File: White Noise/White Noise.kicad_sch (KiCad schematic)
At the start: 7 parts, among them J101 Conn_02x05_Odd_Even

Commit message: Finish main set of revisions
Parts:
- removed C101, C102: 1u, Capacitor_THT:C_Disc_D5.0mm_W2.5mm_P5.00mm, symbol Device:C
- removed D101, D102: 1N5819, Diode_THT:D_DO-41_SOD81_P10.16mm_Horizontal, symbol Diode:1N5819
- removed J101: Conn_02x05_Odd_Even, Connector_PinHeader_2.54mm:PinHeader_2x05_P2.54mm_Vertical, symbol Connector_Generic:Conn_02x05_Odd_Even
- removed R101, R102: 10, Resistor_THT:R_Axial_DIN0207_L6.3mm_D2.5mm_P7.62mm_Horizontal, symbol Device:R
- added C1, C2: 10u, 0_Capacitor_THT:C_Disc_D5.5mm_W4.0mm_P2.50mm, symbol Device:C
- added C3, C4: 0.1u, 0_Capacitor_THT:C_Disc_D5.5mm_W2.5mm_P2.50mm, symbol Device:C
- added C5: 100u, Capacitor_THT:CP_Radial_D5.0mm_P2.00mm, symbol Device:C_Polarized
- added C6: 10n, 0_Capacitor_THT:C_Disc_D5.5mm_W2.5mm_P2.50mm, symbol Device:C
- added C7, C8: 220n, 0_Capacitor_THT:C_Disc_D5.5mm_W2.5mm_P2.50mm, symbol Device:C
- added D1, D2: 1N5819, Diode_THT:D_DO-41_SOD81_P10.16mm_Horizontal, symbol Diode:1N5819
- added J1: Conn_02x05_Top_Bottom, Connector_Molex:Molex_Mini-Fit_Jr_5566-10A_2x05_P4.20mm_Vertical, symbol Connector_Generic:Conn_02x05_Top_Bottom
- added J2: AudioJack2_SwitchT, Connector_Audio:Jack_3.5mm_QingPu_WQP-PJ398SM_Vertical_CircularHoles, symbol Connector_Audio:AudioJack2_SwitchT
- added Q1: BC548, Package_TO_SOT_THT:TO-92_HandSolder, symbol Transistor_BJT:BC548
- added R1, R4, R6: 4.7k, Resistor_THT:R_Axial_DIN0207_L6.3mm_D2.5mm_P7.62mm_Horizontal, symbol Device:R
- added R2, R3, R5: 100k, Resistor_THT:R_Axial_DIN0207_L6.3mm_D2.5mm_P7.62mm_Horizontal, symbol Device:R
- added R7: 1k, Resistor_THT:R_Axial_DIN0207_L6.3mm_D2.5mm_P7.62mm_Horizontal, symbol Device:R
- added RV1: 50k, 0_Potentiometer_THT:Potentiometer_Alpha_RD901F-40-00D_Single_Vertical_MP, symbol Device:R_Potentiometer_MountingPin
- added U1: TL072, Package_DIP:DIP-8_W7.62mm_Socket, symbol Amplifier_Operational:TL072
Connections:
- net +12V: now also C1.1, C3.2, D1.1 (K), J1.1 (Pin_1), J1.6 (Pin_6), R1.1, U1.8 (V+)
- net -12V: now also C2.2, C4.1, D2.2 (A), J1.10 (Pin_10), J1.5 (Pin_5), U1.4 (V-)
- net GND: now also C1.2, C2.1, C3.1, C4.2, C5.2, C7.1, C8.1, D1.2 (A), D2.1 (K), J1.2 (Pin_2), J1.4 (Pin_4), J1.7 (Pin_7), J1.9 (Pin_9), Q1.2 (B), R3.2
- new net: C5.1, R1.2, R2.1
- new net: C7.2, R4.2
- new net: R4.1, R5.1, U1.2 (-)
- new net: C6.1, Q1.3 (E), R2.2
- new net: R6.1, RV1.1, U1.6 (-)
- new net: R7.1, RV1.2, RV1.3, U1.7
- new net: C8.2, R6.2
- new net: J2.T, R7.2
- new net: R5.2, U1.1, U1.5 (+)
- new net: C6.2, R3.1, U1.3 (+)
- new net Chassis: J1.3 (Pin_3), J1.8 (Pin_8), J2.S, RV1.MP (MountPin)
- no-connect marks 0 -> 2
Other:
- removed sheet Single Source 1

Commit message: Begin revised delay
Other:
- moved on the sheet: C1, C2, C3, C4, C5, C6, C7, C8, D1, D2, J1, J2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

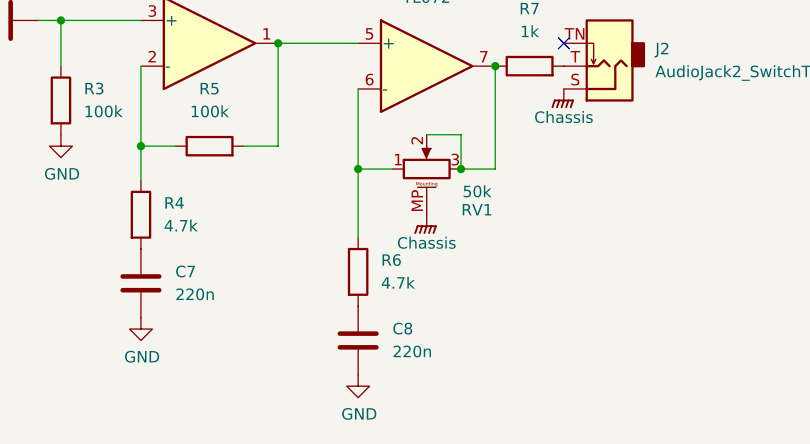
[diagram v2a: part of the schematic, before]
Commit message: Finish diode ladder filter
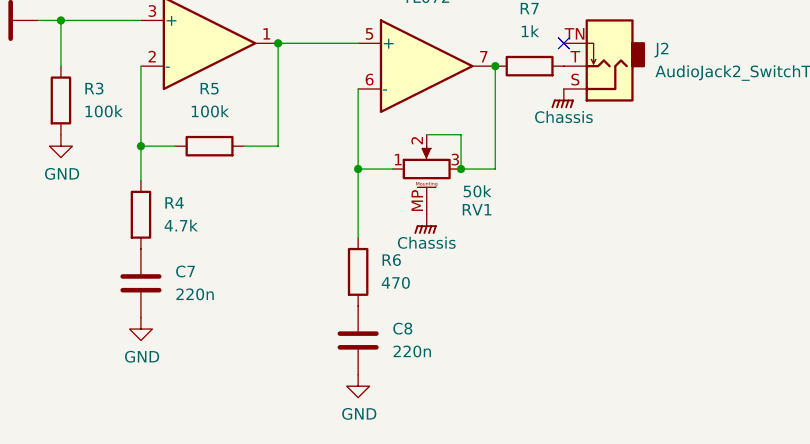
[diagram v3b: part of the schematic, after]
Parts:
- R6: value 4.7k -> 470
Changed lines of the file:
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@@
 			)
 		)
-		(property "Value" "4.7k"
+		(property "Value" "470"
 			(at 156.21 142.2399 0)
 			(effects
